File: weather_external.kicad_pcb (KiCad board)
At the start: 2 copper layers, 28.2 x 33.8 mm, 13 parts, among them J1 Conn_01x02_Male, J2 Conn_01x02_Male, SW1 SW_Push

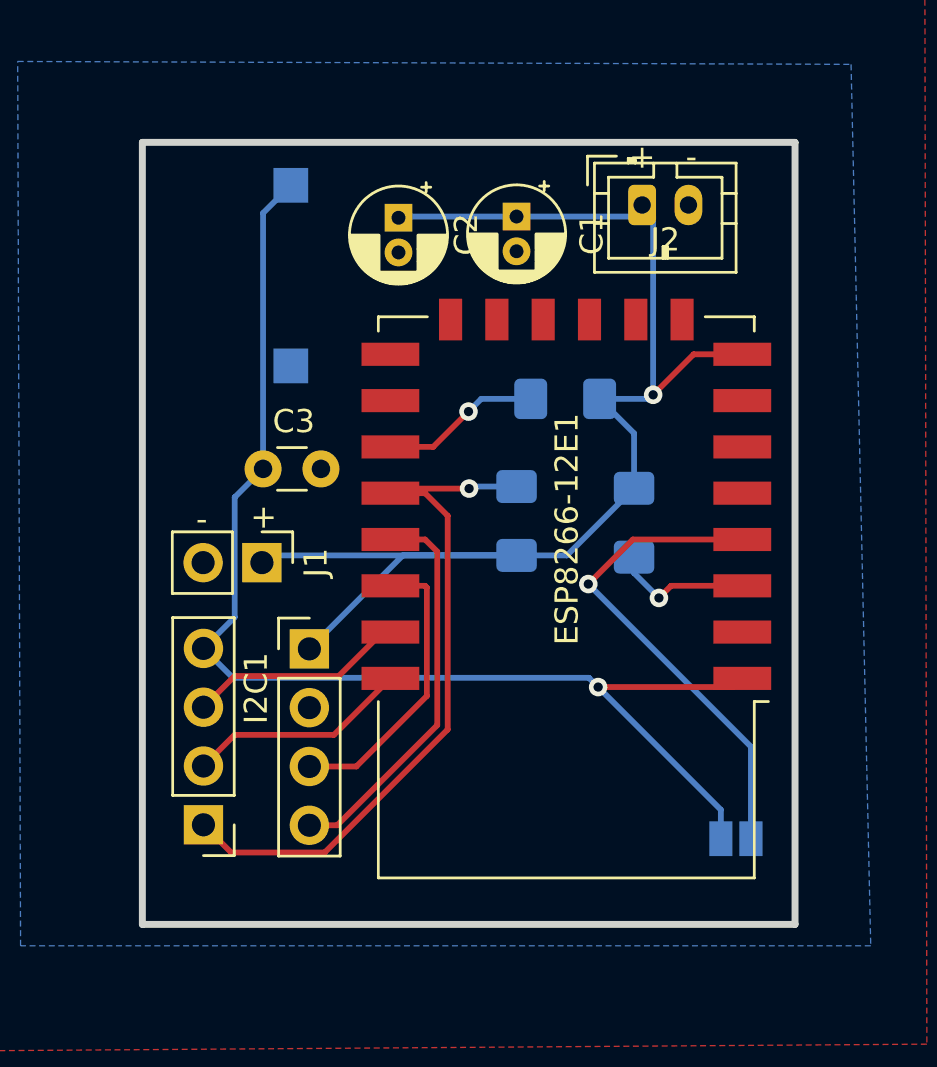
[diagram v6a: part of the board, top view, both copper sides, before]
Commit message: No 555 jlcpcb 1206 resistors
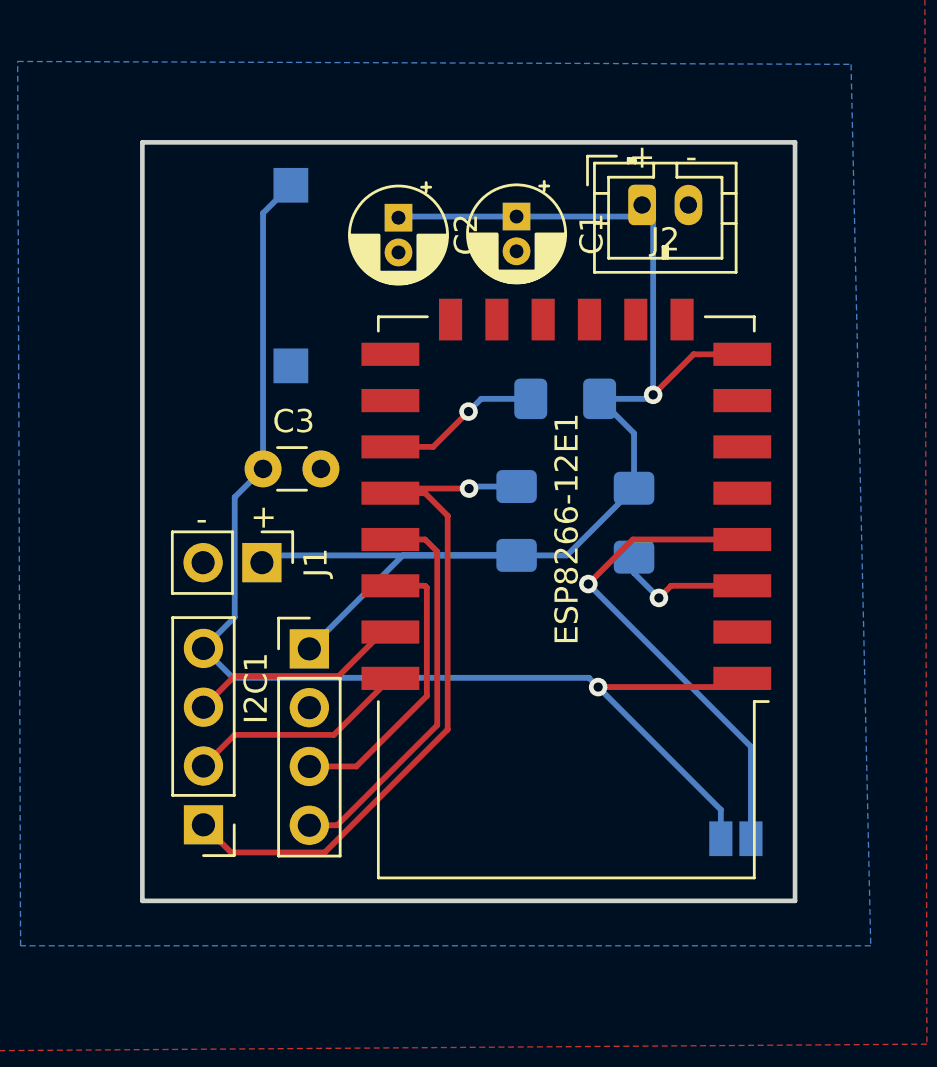
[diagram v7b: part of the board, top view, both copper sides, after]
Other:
- board size 28.2 x 33.8 mm -> 28.2 x 32.8 mm

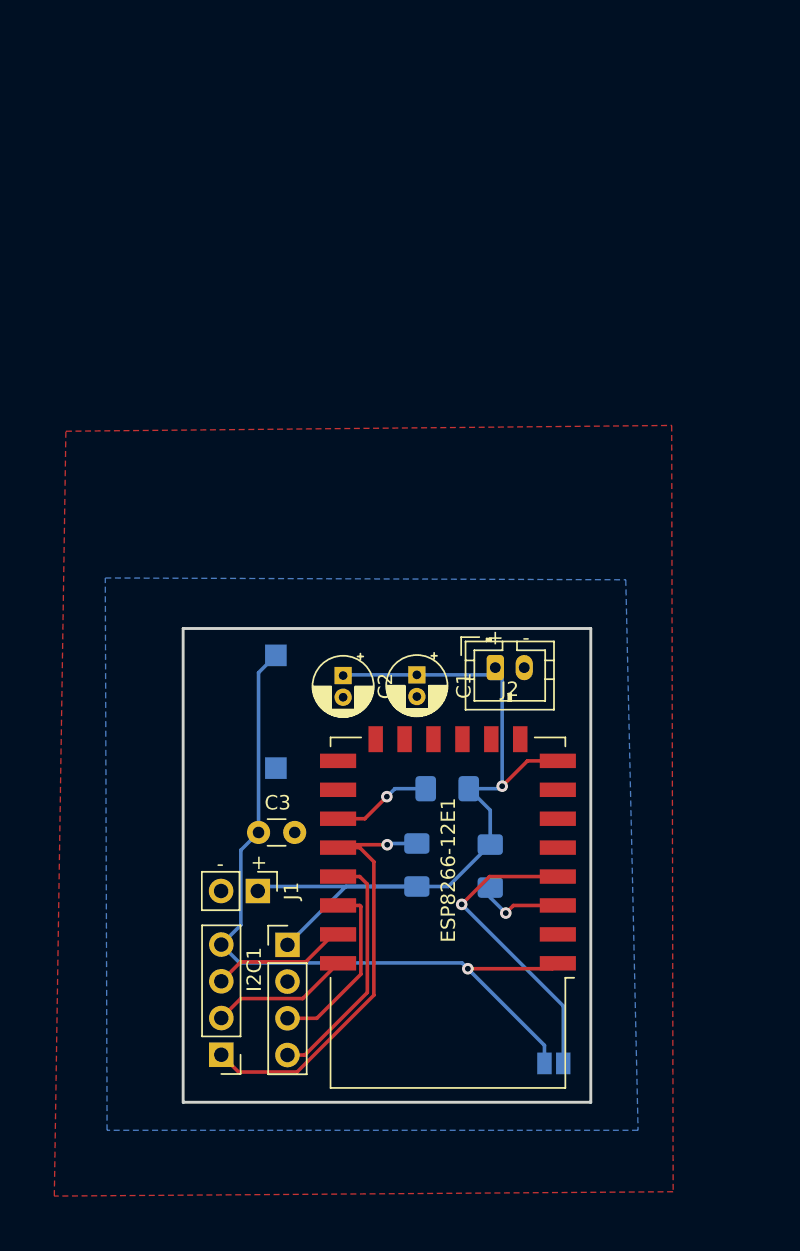
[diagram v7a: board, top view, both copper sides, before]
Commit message: - Adding charger module TP4056 - add usb
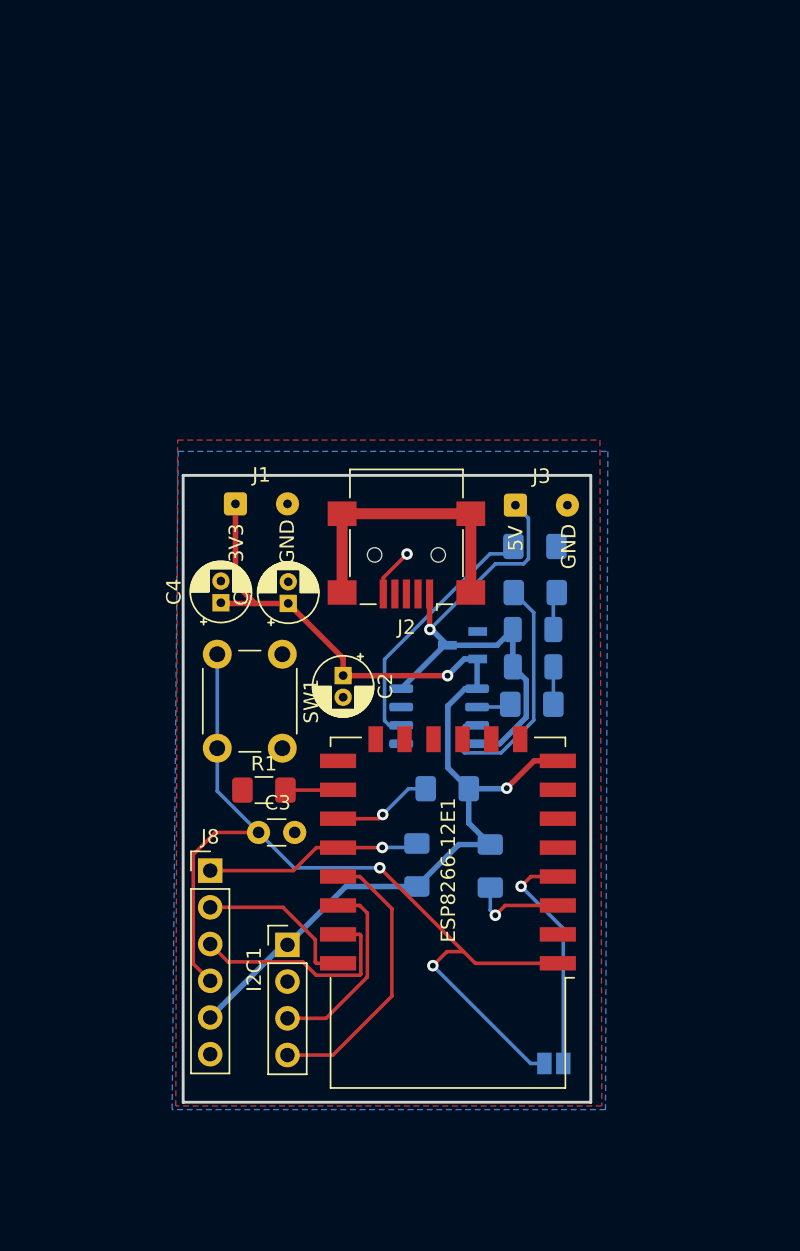
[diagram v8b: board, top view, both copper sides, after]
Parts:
- removed FTDI1: Conn_01x04_Male, Connector_PinHeader_2.54mm:PinHeader_1x04_P2.54mm_Vertical
- added C4: CP, Capacitor_THT:CP_Radial_D4.0mm_P1.50mm, F.Cu at (-1.46, 63.0)
- added D1: LED, LED_SMD:LED_1206_3216Metric, B.Cu at (20.1, 64.8)
- added D2: LED, LED_SMD:LED_1206_3216Metric, B.Cu at (20.1, 67.4)
- added J3: Conn_01x02_Male, Connector_Wire:SolderWire-0.1sqmm_1x02_P3.6mm_D0.4mm_OD1mm, F.Cu at (18.9, 56.2)
- added J8: FTDI, Connector_PinHeader_2.54mm:PinHeader_1x06_P2.54mm_Vertical, F.Cu at (-2.19, 81.5)
- added R1: 10k, Resistor_SMD:R_1206_3216Metric_Pad1.42x1.75mm_HandSolder, F.Cu at (1.52, 75.9)
- added R5: 1k, Resistor_SMD:R_1206_3216Metric_Pad1.42x1.75mm_HandSolder, B.Cu at (20.3, 62.3)
- added R6: 1k, Resistor_SMD:R_1206_3216Metric_Pad1.42x1.75mm_HandSolder, B.Cu at (20.1, 70.0)
- added R7: 1k2, Resistor_SMD:R_1206_3216Metric_Pad1.42x1.75mm_HandSolder, B.Cu at (20.3, 59.1)
- added U1: TP4056, Package_SO:SOP-8_3.9x4.9mm_P1.27mm, B.Cu at (13.6, 70.8)
- added U2: MCP1700T-3302E_TT, digikey-footprints:SOT-23-3, B.Cu at (15.3, 65.9)
- J1: footprint Connector_PinHeader_2.54mm:PinHeader_1x02_P2.54mm_Vertical -> Connector_Wire:SolderWire-0.1sqmm_1x02_P3.6mm_D0.4mm_OD1mm
- J2: value Conn_01x02_Male -> USB_B_Mini; footprint Connector_JST:JST_PH_B2B-PH-K_1x02_P2.00mm_Vertical -> Connector_USB:USB_Mini-B_Lumberg_2486_01_Horizontal
- SW1: footprint Button_Switch_SMD:SW_SPST_CK_RS282G05A3 -> Button_Switch_THT:SW_PUSH_6mm_H4.3mm; moved to F.Cu
- moved J1 26.8 mm to (-0.45, 56.1), turned to 0 degrees
- moved C1 10.2 mm to (3.21, 63.0), turned to 90 degrees
- moved J2 9.93 mm to (11.4, 59.7), turned to 180 degrees
- moved SW1 4.00 mm to (2.79, 66.5), turned to 270 degrees
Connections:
- C1 pad 2: GPIO15 -> GND
- C2 pad 2: GPIO15 -> GND
- C3 pad 1: GPIO15 -> GND
- ESP8266-12E1 pad 15: GPIO15 -> GND
- I2C1 pad 2: GPIO15 -> GND
- J1 pad 2: GPIO15 -> GND
- J2 pad 1: +3V3 -> VCC
- J2 pad 2: GPIO15 -> (no net)
- SW1 pad 1: GPIO15 -> GND
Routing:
- net VCC: track 0.00 -> 37.1 mm, vias 0 -> 1
- net Net-(J2-Pad6): track 0.00 -> 19.8 mm
- net Net-(R7-Pad1): track 0.00 -> 18.1 mm
- net Net-(R5-Pad2): track 0.00 -> 18.1 mm
- net +3V3: track 58.6 -> 75.2 mm, vias 1 -> 2
- net GPIO0: track 30.9 -> 15.1 mm
- net RST: track 54.6 -> 65.4 mm, vias 1 -> 2
- net RX: track 9.42 -> 15.6 mm
- net GPIO16: track 21.4 -> 16.3 mm
- net GPIO15: track 0.00 -> 3.65 mm
- net GND: track 0.00 -> 3.44 mm, vias 0 -> 1
- net Net-(D1-Pad1): track 0.00 -> 2.65 mm
- net Net-(D2-Pad1): track 0.00 -> 2.59 mm
- net SDA: track 17.1 -> 19.6 mm
- net Net-(R6-Pad2): track 0.00 -> 2.38 mm
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- added copper zone on B.Cu, net GND
- added copper zone on F.Cu, net GND
- removed copper zone on B.Cu, net GPIO15
- removed copper zone on F.Cu, net GPIO15
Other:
- board size 28.2 x 32.8 mm -> 28.2 x 43.4 mm
- board text added: "3V3"
- board text added: "5V"
- board text added: "BAT"
- board text added: "GND"
- board text added: "SOLAR PANEL"
